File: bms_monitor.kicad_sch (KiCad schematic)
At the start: 22 parts, among them J1 Conn_01x02, J13 Conn_ARM_JTAG_SWD_10, J2 Conn_01x02, J3 Conn_01x02, J4 Conn_01x02, U1 STM32L432KBUx, U2 MCP1812AT-033-TT, U3 DSC61XX, U4 TFBS4652

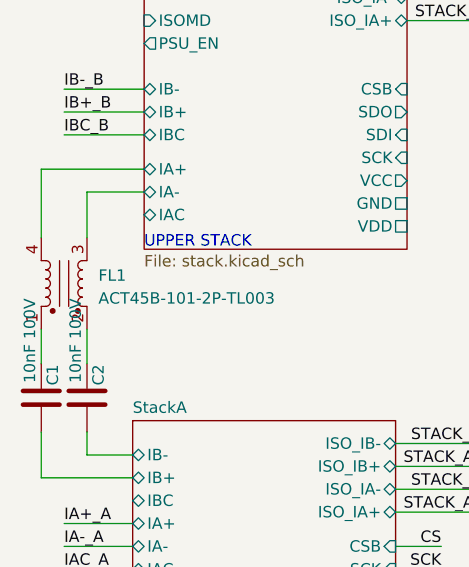
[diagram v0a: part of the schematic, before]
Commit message: Fixed issure #2
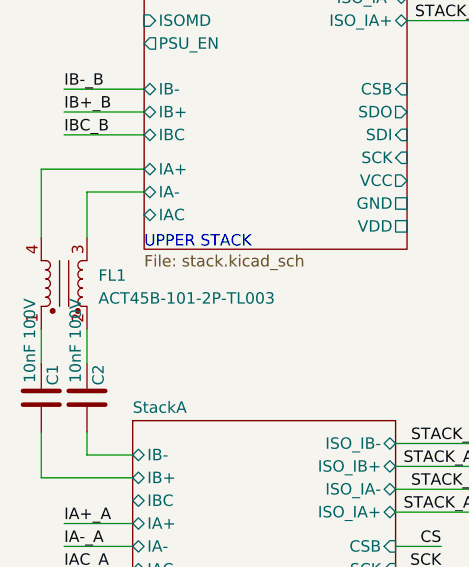
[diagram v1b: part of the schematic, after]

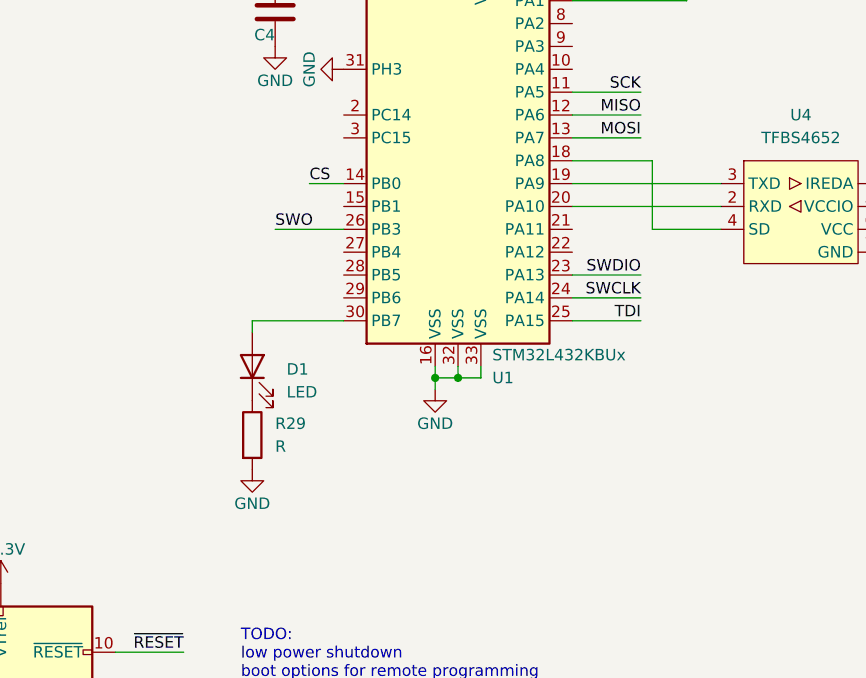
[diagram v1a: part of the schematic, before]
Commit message: changed SWD connector to smd
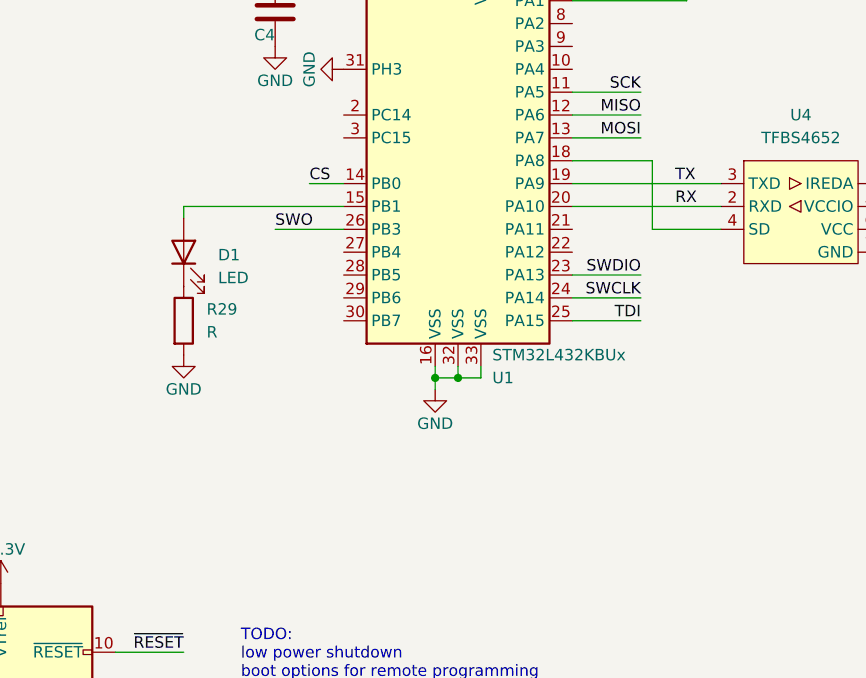
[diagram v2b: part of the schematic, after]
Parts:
- J13: footprint Connector_PinHeader_1.27mm:PinHeader_2x05_P1.27mm_Vertical -> Connector_PinHeader_1.27mm:PinHeader_2x05_P1.27mm_Vertical_SMD
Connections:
- net at D1.2 (A): now also U1.15 (PB1); no longer U1.30 (PB7)
- net RX: now reaches U1.20 (PA10), U4.2 (RXD)
- net TX: now reaches U1.19 (PA9), U4.3 (TXD)
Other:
- moved on the sheet: D1, R29
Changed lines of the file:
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@@
-    (stroke (width 0) (type default))
-  )
-  (wire (pts (xy 180.34 129.54) (xy 190.5 129.54))
     (stroke (width 0) (type default))
   )
@@
     (stroke (width 0) (type default))
   )
-  (wire (pts (xy 180.34 130.81) (xy 180.34 129.54))
+  (wire (pts (xy 172.72 118.11) (xy 172.72 116.84))
     (stroke (width 0) (type default))
   )
@@
   )
   (wire (pts (xy 63.5 109.22) (xy 68.58 109.22))
+    (stroke (width 0) (type default))
+  )
+  (wire (pts (xy 172.72 116.84) (xy 190.5 116.84))
     (stroke (width 0) (type default))
   )
@@
     (effects (font (size 1.27 1.27)) (justify right bottom))
   )
+  (label "RX" (at 227.33 116.84 0) (fields_autoplaced)
+    (effects (font (size 1.27 1.27)) (justify left bottom))
+  )
   (label "STACK_B_IB+" (at 77.47 45.72 180) (fields_autoplaced)
     (effects (font (size 1.27 1.27)) (justify right bottom))
@@
     (effects (font (size 1.27 1.27)) (justify left bottom))
   )
+  (label "TX" (at 227.33 114.3 0) (fields_autoplaced)
+    (effects (font (size 1.27 1.27)) (justify left bottom))
+  )
   (symbol (lib_id "Device:C") (at 182.88 95.25 180) (unit 1)
     (in_bom yes) (on_board yes) (dnp no)
@@
     )
   )
-  (symbol (lib_id "Device:LED") (at 180.34 134.62 90) (unit 1)
+  (symbol (lib_id "Device:LED") (at 172.72 121.92 90) (unit 1)
     (in_bom yes) (on_board yes) (dnp no) (fields_autoplaced)
-    (property "Reference" "D1" (at 184.15 134.9374 90)
+    (property "Reference" "D1" (at 176.53 122.2374 90)
       (effects (font (size 1.27 1.27)) (justify right))
     )
-    (property "Value" "LED" (at 184.15 137.4774 90)
+    (property "Value" "LED" (at 176.53 124.7774 90)
       (effects (font (size 1.27 1.27)) (justify right))
     )
-    (property "Footprint" "LED_SMD:LED_0603_1608Metric" (at 180.34 134.62 0)
-      (effects (font (size 1.27 1.27)) hide)
-    )
-    (property "Datasheet" "~" (at 180.34 134.62 0)
+    (property "Footprint" "LED_SMD:LED_0603_1608Metric" (at 172.72 121.92 0)
+      (effects (font (size 1.27 1.27)) hide)
+    )
+    (property "Datasheet" "~" (at 172.72 121.92 0)
       (effects (font (size 1.27 1.27)) hide)
     )
@@
     )
   )
-  (symbol (lib_id "Device:R") (at 180.34 142.24 0) (unit 1)
+  (symbol (lib_id "Device:R") (at 172.72 129.54 0) (unit 1)
     (in_bom yes) (on_board yes) (dnp no) (fields_autoplaced)
-    (property "Reference" "R29" (at 182.88 140.9699 0)
-      (effects (font (size 1.27 1.27)) (justify left))
-    )
-    (property "Value" "R" (at 182.88 143.5099 0)
-      (effects (font (size 1.27 1.27)) (justify left))
-    )
-    (property "Footprint" "Resistor_SMD:R_0603_1608Metric" (at 178.562 142.24 90)
-      (effects (font (size 1.27 1.27)) hide)
-    )
-    (property "Datasheet" "~" (at 180.34 142.24 0)
+    (property "Reference" "R29" (at 175.26 128.2699 0)
+      (effects (font (size 1.27 1.27)) (justify left))
+    )
+    (property "Value" "R" (at 175.26 130.8099 0)
+      (effects (font (size 1.27 1.27)) (justify left))
+    )
+    (property "Footprint" "Resistor_SMD:R_0603_1608Metric" (at 170.942 129.54 90)
+      (effects (font (size 1.27 1.27)) hide)
+    )
+    (property "Datasheet" "~" (at 172.72 129.54 0)
       (effects (font (size 1.27 1.27)) hide)
     )
@@
     )
   )
-  (symbol (lib_id "power:GND") (at 180.34 146.05 0) (unit 1)
-    (in_bom yes) (on_board yes) (dnp no)
-    (property "Reference" "#PWR0107" (at 180.34 152.4 0)
-      (effects (font (size 1.27 1.27)) hide)
-    )
-    (property "Value" "GND" (at 180.34 149.86 0)
-      (effects (font (size 1.27 1.27)))
-    )
-    (property "Footprint" "" (at 180.34 146.05 0)
-      (effects (font (size 1.27 1.27)) hide)
-    )
-    (property "Datasheet" "" (at 180.34 146.05 0)
+  (symbol (lib_id "power:GND") (at 172.72 133.35 0) (unit 1)
+    (in_bom yes) (on_board yes) (dnp no)
+    (property "Reference" "#PWR0107" (at 172.72 139.7 0)
+      (effects (font (size 1.27 1.27)) hide)
+    )
+    (property "Value" "GND" (at 172.72 137.16 0)
+      (effects (font (size 1.27 1.27)))
+    )
+    (property "Footprint" "" (at 172.72 133.35 0)
+      (effects (font (size 1.27 1.27)) hide)
+    )
+    (property "Datasheet" "" (at 172.72 133.35 0)
       (effects (font (size 1.27 1.27)) hide)
     )
@@
       (effects (font (size 1.27 1.27)) (justify right))
     )
-    (property "Footprint" "Connector_PinHeader_1.27mm:PinHeader_2x05_P1.27mm_Vertical" (at 152.4 173.99 0)
-      (effects (font (size 1.27 1.27)) hide)
-    )
+    (property "Footprint" "Connector_PinHeader_1.27mm:PinHeader_2x05_P1.27mm_Vertical_SMD" (at 152.4 173.99 0)
+      (effects (font (size 1.27 1.27)) hide)
+    )
